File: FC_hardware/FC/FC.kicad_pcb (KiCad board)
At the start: 4 copper layers, 0 parts

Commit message: footprint and PCB outline changes
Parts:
- added C1: 10uF, Capacitor_SMD:C_1206_3216Metric, F.Cu at (164.1, 135.1)
- added C10: 6.8pF, Capacitor_SMD:C_0201_0603Metric, F.Cu at (180.1, 93.7)
- added C11: 0.1uF, Capacitor_SMD:C_0603_1608Metric, F.Cu at (176.9, 90.5)
- added C12: 0.1uF, Capacitor_SMD:C_0603_1608Metric, F.Cu at (176.9, 93.0)
- added C13: 0.1uF, Capacitor_SMD:C_0603_1608Metric, F.Cu at (176.9, 95.6)
- added C14: 0.1uF, Capacitor_SMD:C_0603_1608Metric, F.Cu at (176.9, 98.1)
- added C15: 0.1uF, Capacitor_SMD:C_0603_1608Metric, F.Cu at (176.9, 100.6)
- added C16: 0.1uF, Capacitor_SMD:C_0603_1608Metric, F.Cu at (176.9, 103.1)
- added C17: 0.1uF, Capacitor_SMD:C_0603_1608Metric, F.Cu at (176.9, 105.6)
- added C2: 1uF, Capacitor_SMD:C_0805_2012Metric, F.Cu at (142.9, 112.7)
- added C3: 6.8nF, Capacitor_SMD:C_0201_0603Metric, F.Cu at (180.1, 90.2)
- added C4: 47uF, Capacitor_Tantalum_SMD:CP_EIA-3528-12_Kemet-T, F.Cu at (158.3, 129.7)
- added C5: 47uF, Capacitor_Tantalum_SMD:CP_EIA-3528-12_Kemet-T, F.Cu at (158.3, 134.0)
- added C6: 1uF, Capacitor_SMD:C_0805_2012Metric, F.Cu at (142.9, 115.7)
- added C7: 1uF, Capacitor_SMD:C_0805_2012Metric, F.Cu at (142.9, 118.7)
- added C8: 1uF, Capacitor_SMD:C_0805_2012Metric, F.Cu at (142.9, 121.7)
- added C9: 6.8pF, Capacitor_SMD:C_0201_0603Metric, F.Cu at (180.1, 91.9)
- added D1: B320, Diode_SMD:D_SMA, F.Cu at (145.8, 126.3)
- added D2: Power-Red, LED_SMD:LED_0805_2012Metric, F.Cu at (181.1, 103.0)
- added D3: Status-Green, LED_SMD:LED_0805_2012Metric, F.Cu at (181.1, 106.1)
- added F1: 4A, Fuse:Fuse_0805_2012Metric, F.Cu at (147.4, 121.0)
- added J1: Pin_01x04, Connector_PinHeader_1.27mm:PinHeader_1x04_P1.27mm_Vertical, F.Cu at (172.7, 110.0)
- added J10: GND, footprints:1.27mm_pin, F.Cu at (148.0, 86.1)
- added J11: GND, footprints:1.27mm_pin, F.Cu at (148.1, 89.6)
- added J12: GND, footprints:1.27mm_pin, F.Cu at (148.0, 93.7)
- added J13: Pin_02x03, Connector_PinHeader_1.27mm:PinHeader_2x03_P1.27mm_Vertical, F.Cu at (150.3, 132.6)
- added J14: Pin_01x03, Connector_PinHeader_1.27mm:PinHeader_1x03_P1.27mm_Vertical, F.Cu at (163.4, 129.2)
- added J15: Pin_01x03, Connector_PinHeader_1.27mm:PinHeader_1x03_P1.27mm_Vertical, F.Cu at (167.5, 129.2)
- added J16: PB2, footprints:1.27mm_pin, F.Cu at (147.8, 96.7)
- added J17: PC9, footprints:1.27mm_pin, F.Cu at (147.8, 100.7)
- added J18: PC8, footprints:1.27mm_pin, F.Cu at (147.7, 105.2)
- added J19: PB7, footprints:1.27mm_pin, F.Cu at (150.8, 86.0)
- added J2: USB4105GFA120, footprints:GCT_USB4105GFA120, F.Cu at (112.1, 132.1)
- added J20: PB6, footprints:1.27mm_pin, F.Cu at (150.3, 89.6)
- added J21: PA8, footprints:1.27mm_pin, F.Cu at (150.2, 93.7)
- added J22: PC11, footprints:1.27mm_pin, F.Cu at (150.0, 96.7)
- added J23: PC10, footprints:1.27mm_pin, F.Cu at (150.1, 100.7)
- added J24: PC12, footprints:1.27mm_pin, F.Cu at (149.9, 105.2)
- added J25: PB10, footprints:1.27mm_pin, F.Cu at (153.1, 86.0)
- added J26: PC7, footprints:1.27mm_pin, F.Cu at (152.6, 89.6)
- added J27: PC6, footprints:1.27mm_pin, F.Cu at (152.5, 93.7)
- added J3: 530480810, footprints:MOLEX_530480810, F.Cu at (129.2, 121.0)
- added J4: BAT, footprints:1.27mm_pin, F.Cu at (145.3, 86.0)
- added J5: 5V, footprints:1.27mm_pin, F.Cu at (145.8, 89.6)
- added J6: 5V, footprints:1.27mm_pin, F.Cu at (145.8, 93.7)
- added J7: 3V3, footprints:1.27mm_pin, F.Cu at (145.5, 96.7)
- added J8: 3V3, footprints:1.27mm_pin, F.Cu at (145.6, 100.7)
- added J9: GND, footprints:1.27mm_pin, F.Cu at (145.4, 105.2)
- added JP1: BOOT0, Jumper:SolderJumper-2_P1.3mm_Bridged_RoundedPad1.0x1.5mm, F.Cu at (177.0, 110.1)
- added JP2: ESC_TEL, Jumper:SolderJumper-2_P1.3mm_Open_RoundedPad1.0x1.5mm, F.Cu at (177.0, 113.7)
- added L1: 4.7uH, Inductor_SMD:L_Cenker_CKCS5040, F.Cu at (196.1, 96.7)
- added Q1: BC807W, Package_TO_SOT_SMD:SOT-323_SC-70, F.Cu at (182.3, 133.9)
- added R1: 40.2k, Resistor_SMD:R_0201_0603Metric, F.Cu at (180.1, 95.4)
- added R10: 1k, Resistor_SMD:R_0201_0603Metric, F.Cu at (182.6, 98.9)
- added R11: 4.7k, Resistor_SMD:R_0201_0603Metric, F.Cu at (182.6, 100.7)
- added R12: 40.2k, Resistor_SMD:R_0201_0603Metric, F.Cu at (185.0, 90.2)
- added R13: 1k, Resistor_SMD:R_0201_0603Metric, F.Cu at (185.0, 91.9)
- added R14: 1k, Resistor_SMD:R_0201_0603Metric, F.Cu at (185.0, 93.7)
- added R15: 4.7k, Resistor_SMD:R_0201_0603Metric, F.Cu at (185.0, 95.4)
- added R16: 4.7k, Resistor_SMD:R_0201_0603Metric, F.Cu at (185.0, 97.2)
- added R17: 1k, Resistor_SMD:R_0201_0603Metric, F.Cu at (185.0, 98.9)
- added R18: 1k, Resistor_SMD:R_0201_0603Metric, F.Cu at (185.0, 100.7)
- added R2: 7.68k, Resistor_SMD:R_0201_0603Metric, F.Cu at (180.1, 97.2)
- added R3: 15k, Resistor_SMD:R_0201_0603Metric, F.Cu at (180.1, 98.9)
- added R4: 20R, Resistor_SMD:R_0201_0603Metric, F.Cu at (180.1, 100.7)
- added R5: 604k, Resistor_SMD:R_0201_0603Metric, F.Cu at (182.6, 90.2)
- added R6: 4.7k, Resistor_SMD:R_0201_0603Metric, F.Cu at (182.6, 91.9)
- added R7: 4.7k, Resistor_SMD:R_0201_0603Metric, F.Cu at (182.6, 93.7)
- added R8: 5.1k, Resistor_SMD:R_0201_0603Metric, F.Cu at (182.6, 95.4)
- added R9: 5.1k, Resistor_SMD:R_0201_0603Metric, F.Cu at (182.6, 97.2)
- added REF**: MountingHole_2.2mm_M2, MountingHole:MountingHole_2.2mm_M2, F.Cu at (104.2, 104.2)
- added REF**1: MountingHole_2.2mm_M2, MountingHole:MountingHole_2.2mm_M2, F.Cu at (129.8, 104.2)
- added REF**2: MountingHole_2.2mm_M2, MountingHole:MountingHole_2.2mm_M2, F.Cu at (104.2, 129.8)
- added REF**3: MountingHole_2.2mm_M2, MountingHole:MountingHole_2.2mm_M2, F.Cu at (129.8, 129.8)
- added S1: EVQ-P7L01P, footprints:SW_EVQ-P7L01P, F.Cu at (144.9, 133.2)
- added U1: MP2348, Package_TO_SOT_SMD:SOT-583-8, F.Cu at (153.4, 125.2)
- added U2: AMS1117-3.3, Package_TO_SOT_SMD:SOT-223-3_TabPin2, F.Cu at (150.1, 115.4)
- added U3: STM32F446RETx, Package_QFP:LQFP-64_10x10mm_P0.5mm, F.Cu at (199.1, 112.0)
- added U4: MPU-9250, Sensor_Motion:InvenSense_QFN-24_3x3mm_P0.4mm, F.Cu at (177.6, 134.4)
- added U5: DPS368XTSA1, footprints:XDCR_DPS368XTSA1, F.Cu at (188.9, 101.8)
- added U6: Ai-Thinker-Ra-02, RF_Module:Ai-Thinker-Ra-01-LoRa, F.Cu at (117.4, 114.2)
- added Y1: ABM8G-25MHZ, footprints:XTAL_ABM8G-25.000MHZ-4Y-T3, F.Cu at (172.8, 134.4)
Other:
- board outline added: 34 x 34 mm

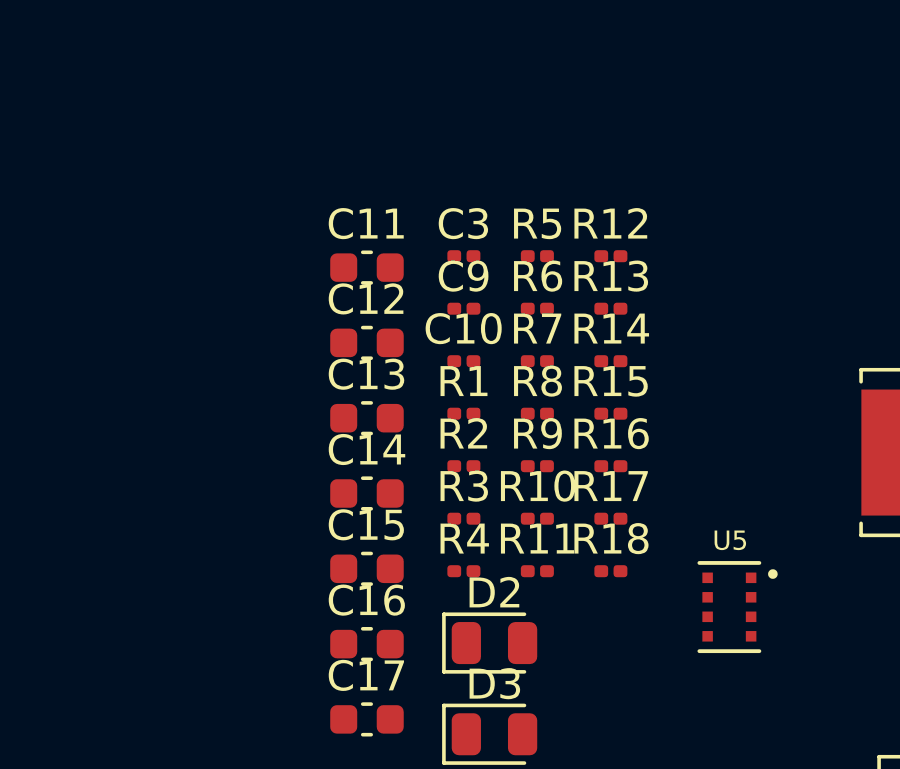
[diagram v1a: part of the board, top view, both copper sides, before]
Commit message: fixup! 0201 changed to 0603
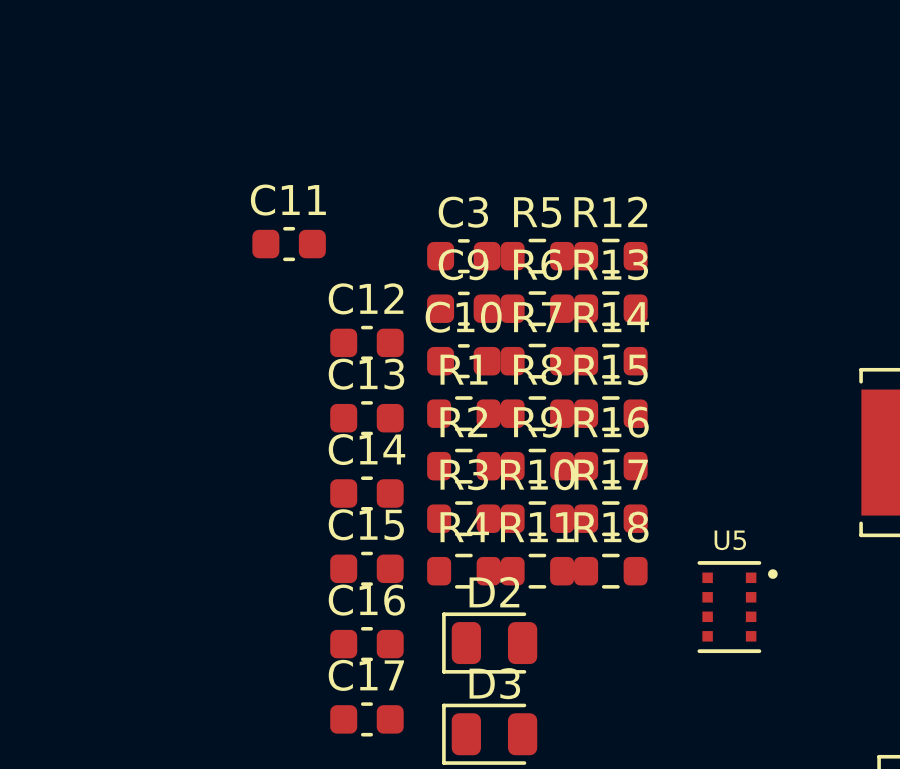
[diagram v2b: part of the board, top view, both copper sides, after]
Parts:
- C10, C3, C9: footprint Capacitor_SMD:C_0201_0603Metric -> Capacitor_SMD:C_0603_1608Metric
- R1, R10, R11, R12, R13, R14, R15, R16, R17, R18, R2, R3, R4, R5, R6, R7, R8, R9: footprint Resistor_SMD:R_0201_0603Metric -> Resistor_SMD:R_0603_1608Metric
- moved C11 2.71 mm to (174.3, 89.8)

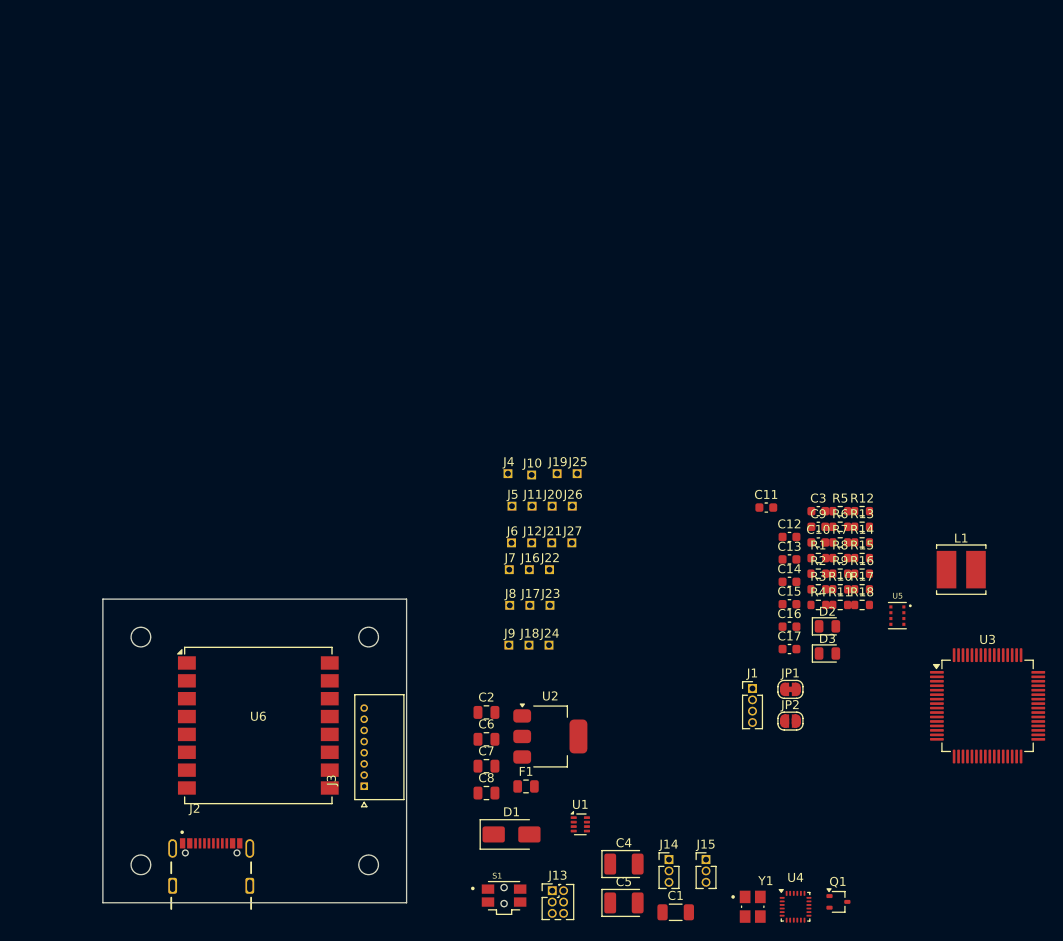
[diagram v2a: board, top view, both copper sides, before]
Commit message: Pin config changed, LoRa module removed from board
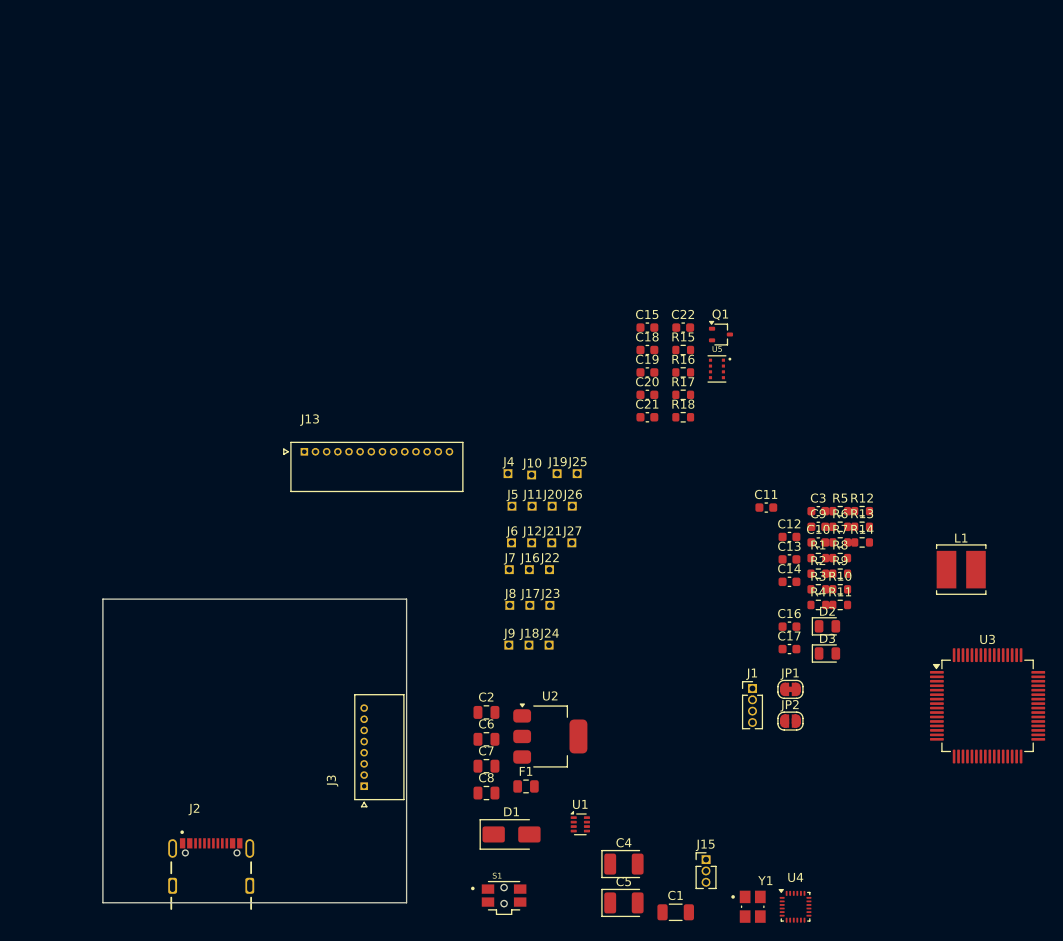
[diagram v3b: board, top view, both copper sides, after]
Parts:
- removed J14: Pin_01x03, Connector_PinHeader_1.27mm:PinHeader_1x03_P1.27mm_Vertical
- removed REF**, REF**1, REF**2, REF**3: MountingHole_2.2mm_M2, MountingHole:MountingHole_2.2mm_M2
- removed U6: Ai-Thinker-Ra-02, RF_Module:Ai-Thinker-Ra-01-LoRa
- added C18: 0.1uF, Capacitor_SMD:C_0603_1608Metric, F.Cu at (161.0, 72.1)
- added C19: 0.1uF, Capacitor_SMD:C_0603_1608Metric, F.Cu at (161.0, 74.6)
- added C20: 0.1uF, Capacitor_SMD:C_0603_1608Metric, F.Cu at (161.0, 77.1)
- added C21: 0.1uF, Capacitor_SMD:C_0603_1608Metric, F.Cu at (161.0, 79.6)
- added C22: 0.1uF, Capacitor_SMD:C_0603_1608Metric, F.Cu at (165.0, 69.6)
- J13: value Pin_02x03 -> 530481410; footprint Connector_PinHeader_1.27mm:PinHeader_2x03_P1.27mm_Vertical -> footprints:MOLEX_530481410
- moved Q1 64.9 mm to (169.2, 70.4)
- moved J13 56.4 mm to (122.5, 83.5)
- moved C15 34.8 mm to (161.0, 69.6)
- moved U5 34.2 mm to (168.8, 74.2)
- moved R15 30.7 mm to (165.0, 72.1)
- moved R16 30.2 mm to (165.0, 74.6)
- moved R17 29.6 mm to (165.0, 77.1)
- moved R18 29.0 mm to (165.0, 79.6)
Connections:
- net Net-(D3-A) renamed /LED
- net Net-(JP1-B) renamed /BOOT
- net Net-(JP2-B) renamed /ESC_RX_MCU
- net Net-(U1-SW) renamed /SW
- net Net-(U1-VIN) renamed /BAT_VIN
- net Net-(U3-NRST) renamed /NRST
- net Net-(U3-PH0) renamed /OSC_IN
- net Net-(U3-PH1) renamed /OSC_OUT
- net Net-(U3-VCAP_1) renamed /VCAP_1
- C14 pad 1: 3V3 -> 5V
- C15 pad 1: 3V3 -> GND
- C15 pad 2: GND -> 3V3
- J13 pad 2: 5V -> 3V3
- J13 pad 3: /GPS_RX -> 5V
- J13 pad 4: /GPS_TX -> Net-(J13-SBUS_RX)
- J13 pad 5: /MAG_SCL -> /GPS_TX
- J13 pad 6: /MAG_SDA -> /GPS_RX
- R17 pad 1: Net-(Q1-B) -> GND
- R17 pad 2: Net-(J14-SBUS) -> /SBUS_RX
- R18 pad 1: GND -> Net-(Q1-B)
- R18 pad 2: /SBUS_RX -> Net-(J13-SBUS_RX)
- U3 pad 10: /ADC_I -> unconnected-(U3-PC2-Pad10)
- U3 pad 20: /LORA_NSS -> /LORA_RST
- U3 pad 21: /LORA_RST -> /IMU_BAR_SCK
- U3 pad 34: /LORA_BAR_SCK -> /LORA_SCK
- U3 pad 35: /LORA_BAR_MISO -> /LORA_MISO
- U3 pad 36: /LORA_BAR_MOSI -> /LORA_MOSI
- U3 pad 50: unconnected-(U3-PA15-Pad50) -> /IMU_CS
- U3 pad 51: /GEN_SCK -> unconnected-(U3-PC10-Pad51)
- U3 pad 55: /IMU_SCK -> /GEN_SCK
- U3 pad 56: /IMU_MISO -> /IMU_BAR_MISO
- U3 pad 57: /IMU_MOSI -> /IMU_BAR_MOSI
- U3 pad 8: unconnected-(U3-PC0-Pad8) -> /ADC_I
- U4 pad 22: GND -> /IMU_CS
- U4 pad 23: /IMU_SCK -> /IMU_BAR_SCK
- U4 pad 24: /IMU_MOSI -> /IMU_BAR_MOSI
- U4 pad 9: /IMU_MISO -> /IMU_BAR_MISO
- U5 pad 1: GND -> 3V3
- U5 pad 3: /LORA_BAR_MOSI -> /IMU_BAR_MOSI
- U5 pad 4: /LORA_BAR_SCK -> /IMU_BAR_SCK
- U5 pad 5: /LORA_BAR_MISO -> /IMU_BAR_MISO
- U5 pad 6: 3V3 -> GND
- U5 pad 7: GND -> 3V3
- U5 pad 8: 3V3 -> GND

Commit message: Board outline, DRU
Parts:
- added H1: MountingHole, MountingHole:MountingHole_2.2mm_M2, F.Cu at (100.0, 100.0)
- added H2: MountingHole, MountingHole:MountingHole_2.2mm_M2, F.Cu at (125.5, 100.0)
- added H3: MountingHole, MountingHole:MountingHole_2.2mm_M2, F.Cu at (100.0, 125.5)
- added H4: MountingHole, MountingHole:MountingHole_2.2mm_M2, F.Cu at (125.5, 125.5)
- added U6: USBLC6-2SC6, Package_TO_SOT_SMD:SOT-23-6, F.Cu at (118.1, 72.8)
- moved C17 105.2 mm to (96.2, 38.0)
- moved U3 103.9 mm to (113.5, 53.1)
- moved C3 102.2 mm to (92.2, 38.0)
- moved C9 101.8 mm to (92.2, 40.5)
- moved R4 101.5 mm to (100.2, 38.0)
- moved C10 101.4 mm to (92.2, 43.0)
- moved R13 97.1 mm to (104.3, 38.0)
- moved R14 96.7 mm to (104.3, 40.5)
- moved R5 96.1 mm to (100.2, 40.5)
- moved C12 95.9 mm to (92.2, 48.0)
- moved C13 95.9 mm to (92.2, 50.5)
- moved C14 95.9 mm to (92.2, 53.1)
- moved C16 95.9 mm to (92.2, 58.1)
- moved R6 95.7 mm to (100.2, 43.0)
- moved R7 95.3 mm to (100.2, 45.5)
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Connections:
- net 5V renamed +5V
- net BAT renamed +BATT
- net Net-(D1-A) renamed VBUS
- C11 pad 2: 3V3 -> +3V3
- C12 pad 1: 3V3 -> +3V3
- C15 pad 2: 3V3 -> +3V3
- C18 pad 2: 3V3 -> +3V3
- C19 pad 2: 3V3 -> +3V3
- C20 pad 2: 3V3 -> +3V3
- C21 pad 2: 3V3 -> +3V3
- C22 pad 1: 3V3 -> +3V3
- C5 pad 1: 3V3 -> +3V3
- C7 pad 1: 3V3 -> +3V3
- D2 pad 2: 3V3 -> +3V3
- J1 pad 4: 3V3 -> +3V3
- J13 pad 2: 3V3 -> +3V3
- J2 pad A6: /USB_DP -> /USB_DC_P
- J2 pad A7: /USB_DM -> /USB_DC_N
- J2 pad B6: /USB_DP -> /USB_DC_P
- J2 pad B7: /USB_DM -> /USB_DC_N
- J7 pad 1: 3V3 -> +3V3
- J8 pad 1: 3V3 -> +3V3
- Q1 pad 2: 3V3 -> +3V3
- R15 pad 2: 3V3 -> +3V3
- R16 pad 2: 3V3 -> +3V3
- R6 pad 2: 3V3 -> +3V3
- R7 pad 2: 3V3 -> +3V3
- R9 pad 1: GND -> Net-(J2-CC1)
- R9 pad 2: Net-(J2-CC1) -> GND
- S1 pad 1_1: /NRST -> GND
- S1 pad 1_2: /NRST -> GND
- S1 pad 2_1: GND -> /NRST
- S1 pad 2_2: GND -> /NRST
- U2 pad 2: 3V3 -> +3V3
- U3 pad 1: 3V3 -> +3V3
- U3 pad 13: 3V3 -> +3V3
- U3 pad 19: 3V3 -> +3V3
- U3 pad 32: 3V3 -> +3V3
- U3 pad 44: /USB_DM -> /USB_DN
- U3 pad 48: 3V3 -> +3V3
- U3 pad 64: 3V3 -> +3V3
- U4 pad 1: 3V3 -> +3V3
- U4 pad 13: 3V3 -> +3V3
- U4 pad 8: 3V3 -> +3V3
- U5 pad 1: 3V3 -> GND
- U5 pad 6: GND -> +3V3
- U5 pad 7: 3V3 -> GND
- U5 pad 8: GND -> +3V3
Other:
- outline, holes or cut-outs redrawn
